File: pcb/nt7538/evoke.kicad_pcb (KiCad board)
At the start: 2 copper layers, 60 x 45 mm, 42 parts, among them J1 Conn_01x03_Male, J2 BACKLIGHT_CONN, Q1 Q_NMOS_GSD, U1 STM32F103C8Tx

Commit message: More NT7538 tweaks
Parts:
- renumbered INPUT_CONN to INPUT_CONN1, AUX_PWR to J3, LCD_CONN to LCD_CONN1
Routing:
- net GND: track 61.3 -> 56.8 mm, vias 15 -> 14
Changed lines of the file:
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@@
     (thickness 1.6)
     (drawings 19)
-    (tracks 506)
+    (tracks 501)
     (zones 0)
     (modules 42)
@@
     (tags "connector Molex  top entry")
     (attr smd)
-    (fp_text reference INPUT_CONN (at -0.508 5.588) (layer F.SilkS)
+    (fp_text reference INPUT_CONN1 (at -0.508 5.588) (layer F.SilkS)
       (effects (font (size 1 1) (thickness 0.15)))
     )
@@
     (tags "connector Hirose FH12 horizontal")
     (attr smd)
-    (fp_text reference LCD_CONN (at 0 -4.064) (layer F.SilkS)
+    (fp_text reference LCD_CONN1 (at 0 -4.064) (layer F.SilkS)
       (effects (font (size 1 1) (thickness 0.15)))
     )
@@
     (descr "Through hole straight pin header, 1x02, 2.54mm pitch, single row")
     (tags "Through hole pin header THT 1x02 2.54mm single row")
-    (fp_text reference AUX_PWR (at -0.254 5.334) (layer F.SilkS)
+    (fp_text reference J3 (at -0.254 5.334) (layer F.SilkS)
       (effects (font (size 1 1) (thickness 0.15)))
     )
@@
     (descr "Potentiometer, vertical, Vishay T73YP, http://www.vishay.com/docs/51016/t73.pdf")
     (tags "Potentiometer vertical Vishay T73YP")
-    (fp_text reference CONTRAST (at 0 -6.858) (layer F.SilkS)
+    (fp_text reference CONTRAST (at 0.254 -6.858) (layer F.SilkS)
       (effects (font (size 1 1) (thickness 0.15)))
     )
@@
   (segment (start 104.152 38.238) (end 104.152 35.826) (width 0.3) (layer F.Cu) (net 5))
   (segment (start 104.14 35.814) (end 111.76 35.814) (width 0.3) (layer F.Cu) (net 5))
-  (segment (start 100.838 37.448) (end 100.838 35.814) (width 0.3) (layer F.Cu) (net 5))
-  (segment (start 100.91 37.52) (end 100.838 37.448) (width 0.3) (layer F.Cu) (net 5))
-  (segment (start 100.91 39.188) (end 100.91 37.52) (width 0.3) (layer F.Cu) (net 5))
   (segment (start 100.838 35.814) (end 104.14 35.814) (width 0.3) (layer F.Cu) (net 5))
-  (segment (start 98.044 35.814) (end 100.838 35.814) (width 0.3) (layer F.Cu) (net 5))
   (segment (start 100.91 39.188) (end 101.652 39.188) (width 0.25) (layer F.Cu) (net 5))
   (segment (start 102.938002 73.66) (end 94.742 73.66) (width 0.5) (layer F.Cu) (net 5))
@@
   (segment (start 93.6475 47.498) (end 92.8855 48.26) (width 0.25) (layer F.Cu) (net 5))
   (segment (start 95.758 47.498) (end 93.6475 47.498) (width 0.25) (layer F.Cu) (net 5))
+  (segment (start 100.652 35.882) (end 100.584 35.814) (width 0.25) (layer F.Cu) (net 5))
+  (segment (start 100.652 39.188) (end 100.652 35.882) (width 0.25) (layer F.Cu) (net 5))
+  (segment (start 100.584 35.814) (end 100.838 35.814) (width 0.3) (layer F.Cu) (net 5))
+  (segment (start 98.044 35.814) (end 100.584 35.814) (width 0.3) (layer F.Cu) (net 5))
   (segment (start 105.176999 38.277999) (end 106.370998 37.084) (width 0.25) (layer F.Cu) (net 6))
   (segment (start 105.176999 39.163001) (end 105.176999 38.277999) (width 0.25) (layer F.Cu) (net 6))
@@
   (segment (start 107.66 51.344) (end 107.188 51.816) (width 0.25) (layer F.Cu) (net 35))
   (segment (start 110.9195 63.3245) (end 110.998 63.246) (width 0.25) (layer F.Cu) (net 35))
-  (via (at 112.776 64.008) (size 0.8) (drill 0.4) (layers F.Cu B.Cu) (net 35))
-  (segment (start 112.3465 64.4375) (end 112.776 64.008) (width 0.25) (layer F.Cu) (net 35))
-  (segment (start 110.9195 64.4375) (end 112.3465 64.4375) (width 0.25) (layer F.Cu) (net 35))
-  (segment (start 110.9195 64.4375) (end 110.9195 63.3245) (width 0.25) (layer F.Cu) (net 35))
-  (segment (start 110.9195 65.786) (end 110.9195 64.4375) (width 0.25) (layer F.Cu) (net 35))
   (via (at 117.602 45.212) (size 0.8) (drill 0.4) (layers F.Cu B.Cu) (net 35))
   (via (at 99.822 62.992) (size 0.8) (drill 0.4) (layers F.Cu B.Cu) (net 35))

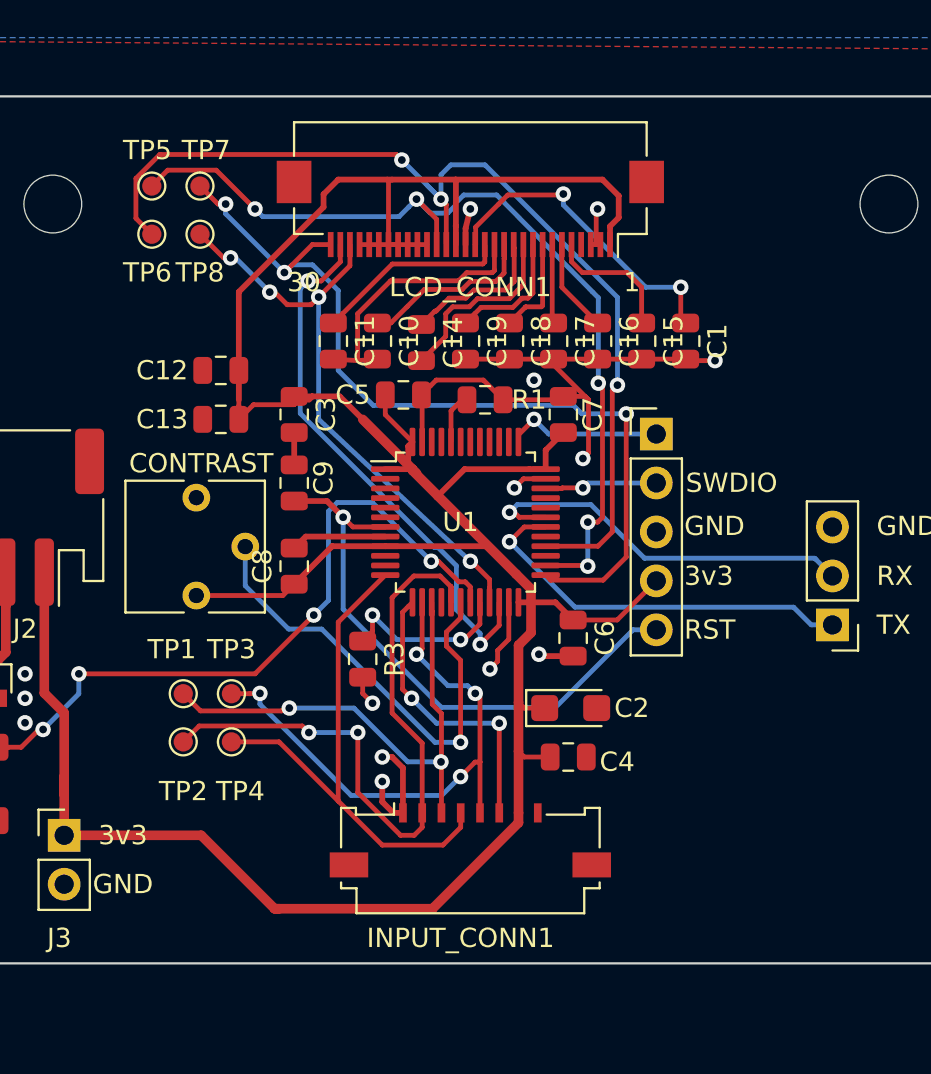
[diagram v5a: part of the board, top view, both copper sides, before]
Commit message: NT7538 to manufacture
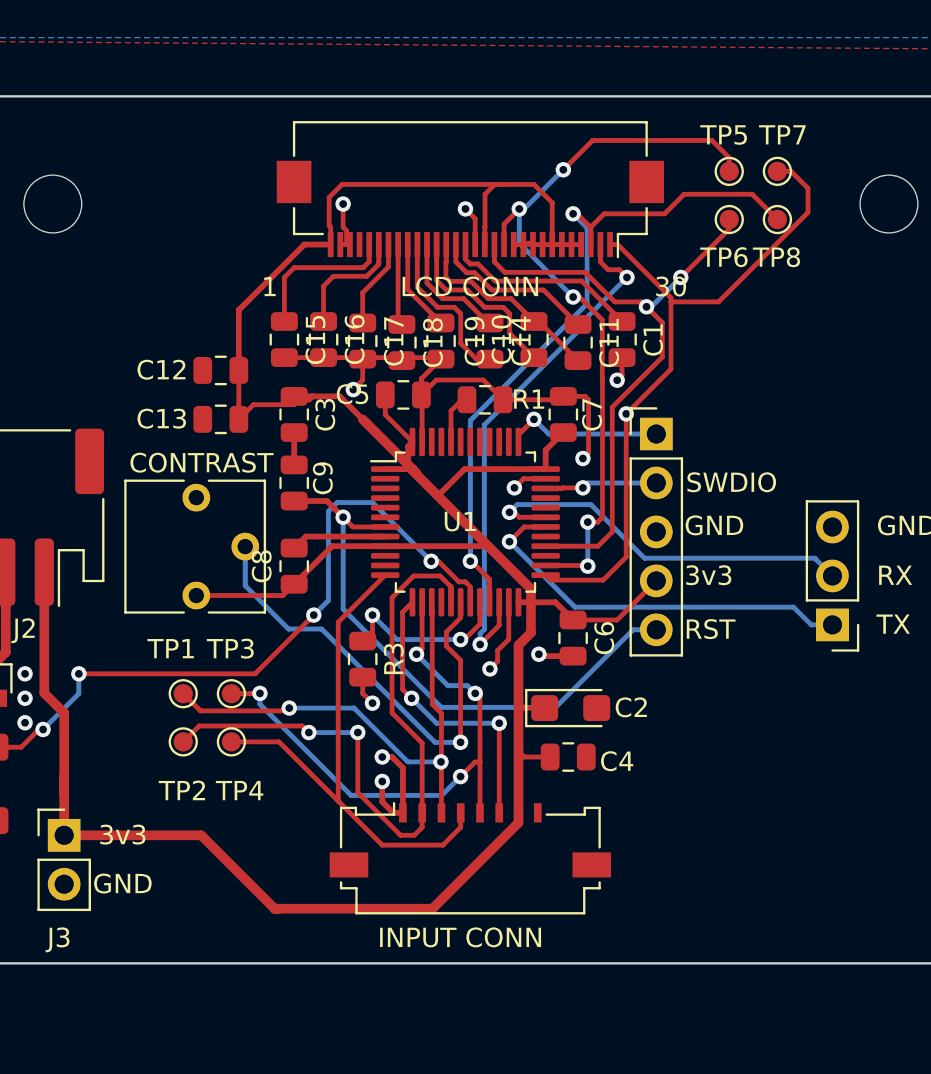
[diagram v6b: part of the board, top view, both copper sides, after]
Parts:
- INPUT CONN: renamed from INPUT_CONN1
- LCD CONN: renamed from LCD_CONN1
- moved TP5 30.0 mm to (118.3, 35.4)
- moved TP6 30.0 mm to (118.3, 37.9)
- moved TP7 30.0 mm to (120.8, 35.4)
- moved TP8 30.0 mm to (120.8, 37.9)
- moved C15 18.5 mm to (95.2, 44.1)
- moved C16 14.2 mm to (97.3, 44.1)
- moved C11 12.7 mm to (110.5, 44.3)
- moved C17 9.91 mm to (99.3, 44.2)
- moved C10 8.13 mm to (108.2, 44.1), turned to 90 degrees
- moved C18 5.59 mm to (101.3, 44.3)
- moved C14 3.56 mm to (105.9, 44.2)
- moved C1 3.30 mm to (112.8, 44.1)
- moved C19 1.27 mm to (103.4, 44.2)
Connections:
- LCD CONN pad 1: +3V3 -> LCD_CS
- LCD CONN pad 10: Net-(C14-Pad2) -> +3V3
- LCD CONN pad 11: Net-(C14-Pad1) -> +3V3
- LCD CONN pad 12: Net-(C10-Pad1) -> LCD_SCK
- LCD CONN pad 13: Net-(C10-Pad2) -> LCD_DATA
- LCD CONN pad 14: Net-(C11-Pad1) -> +3V3
- LCD CONN pad 15: Net-(C1-Pad1) -> GND
- LCD CONN pad 16: GND -> Net-(C1-Pad1)
- LCD CONN pad 17: +3V3 -> Net-(C11-Pad1)
- LCD CONN pad 18: LCD_DATA -> Net-(C10-Pad2)
- LCD CONN pad 19: LCD_SCK -> Net-(C10-Pad1)
- LCD CONN pad 2: GND -> LCD_RST
- LCD CONN pad 20: +3V3 -> Net-(C14-Pad1)
- LCD CONN pad 21: +3V3 -> Net-(C14-Pad2)
- LCD CONN pad 22: +3V3 -> Net-(C19-Pad1)
- LCD CONN pad 23: +3V3 -> Net-(C18-Pad1)
- LCD CONN pad 24: +3V3 -> Net-(C17-Pad1)
- LCD CONN pad 25: +3V3 -> Net-(C16-Pad1)
- LCD CONN pad 26: +3V3 -> Net-(C15-Pad1)
- LCD CONN pad 27: +3V3 -> Net-(LCD_CONN1-Pad27)
- LCD CONN pad 28: LCD_D_C -> GND
- LCD CONN pad 29: LCD_RST -> GND
- LCD CONN pad 3: GND -> LCD_D_C
- LCD CONN pad 30: LCD_CS -> +3V3
- LCD CONN pad 4: Net-(LCD_CONN1-Pad4) -> +3V3
- LCD CONN pad 5: Net-(C15-Pad1) -> +3V3
- LCD CONN pad 6: Net-(C16-Pad1) -> +3V3
- LCD CONN pad 7: Net-(C17-Pad1) -> +3V3
- LCD CONN pad 8: Net-(C18-Pad1) -> +3V3
- LCD CONN pad 9: Net-(C19-Pad1) -> +3V3
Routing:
- net LCD_DATA: track 53.2 -> 33.1 mm, vias 3 -> 2
- net LCD_CS: track 45.3 -> 35.8 mm, vias 3 -> 1
- net LCD_SCK: track 47.6 -> 39.0 mm
- net +3V3: track 165.1 -> 157.2 mm
- net Net-(C1-Pad1): track 16.6 -> 10.2 mm, vias 2 -> 0
- net LCD_D_C: track 30.9 -> 37.0 mm, vias 4 -> 2
- net Net-(C10-Pad2): track 14.1 -> 10.4 mm
- net Net-(C19-Pad1): track 6.67 -> 4.79 mm
- net GND: track 56.8 -> 54.9 mm
- net Net-(C14-Pad1): track 7.67 -> 6.12 mm
- net Net-(C14-Pad2): track 9.92 -> 8.42 mm
- net Net-(C11-Pad1): track 10.1 -> 8.58 mm
- net Net-(C16-Pad1): track 4.84 -> 6.20 mm
- net LCD_RST: track 28.7 -> 27.4 mm
- net Net-(C18-Pad1): track 5.26 -> 4.23 mm
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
